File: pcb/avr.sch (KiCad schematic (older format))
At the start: 33 parts, among them IC201 MCU-ATMEGA328P-MU_QFN32_, J201 CONN_02X03, P201 CONNECTOR, P202 CONNECTOR, P203 CONNECTOR, P204 CONNECTOR, P205 CONNECTOR, P206 CONNECTOR, P207 CONNECTOR, P208 CONNECTOR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

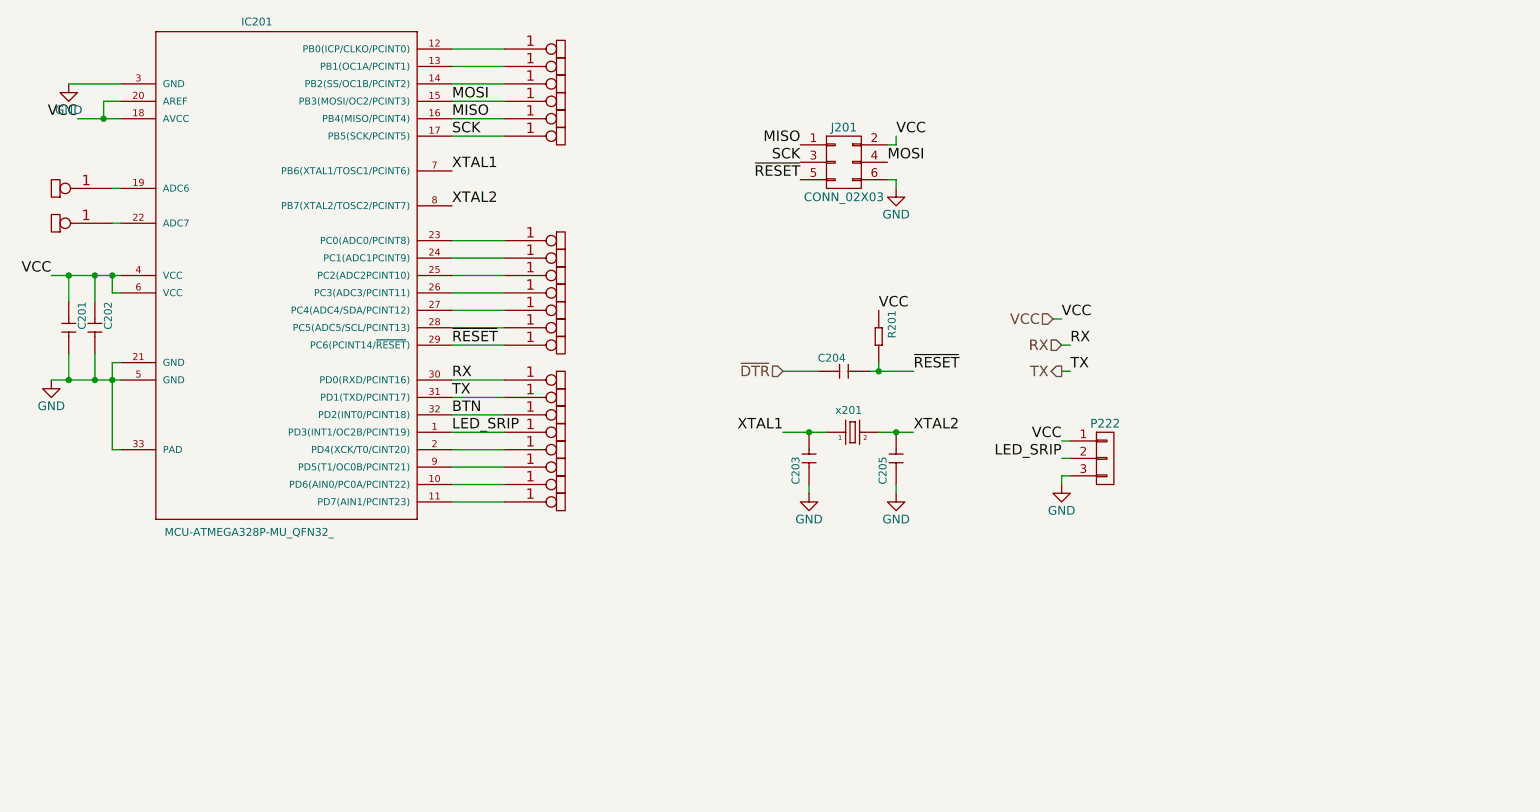
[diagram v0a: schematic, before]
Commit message: added led strip power control, minor adjustments to layout
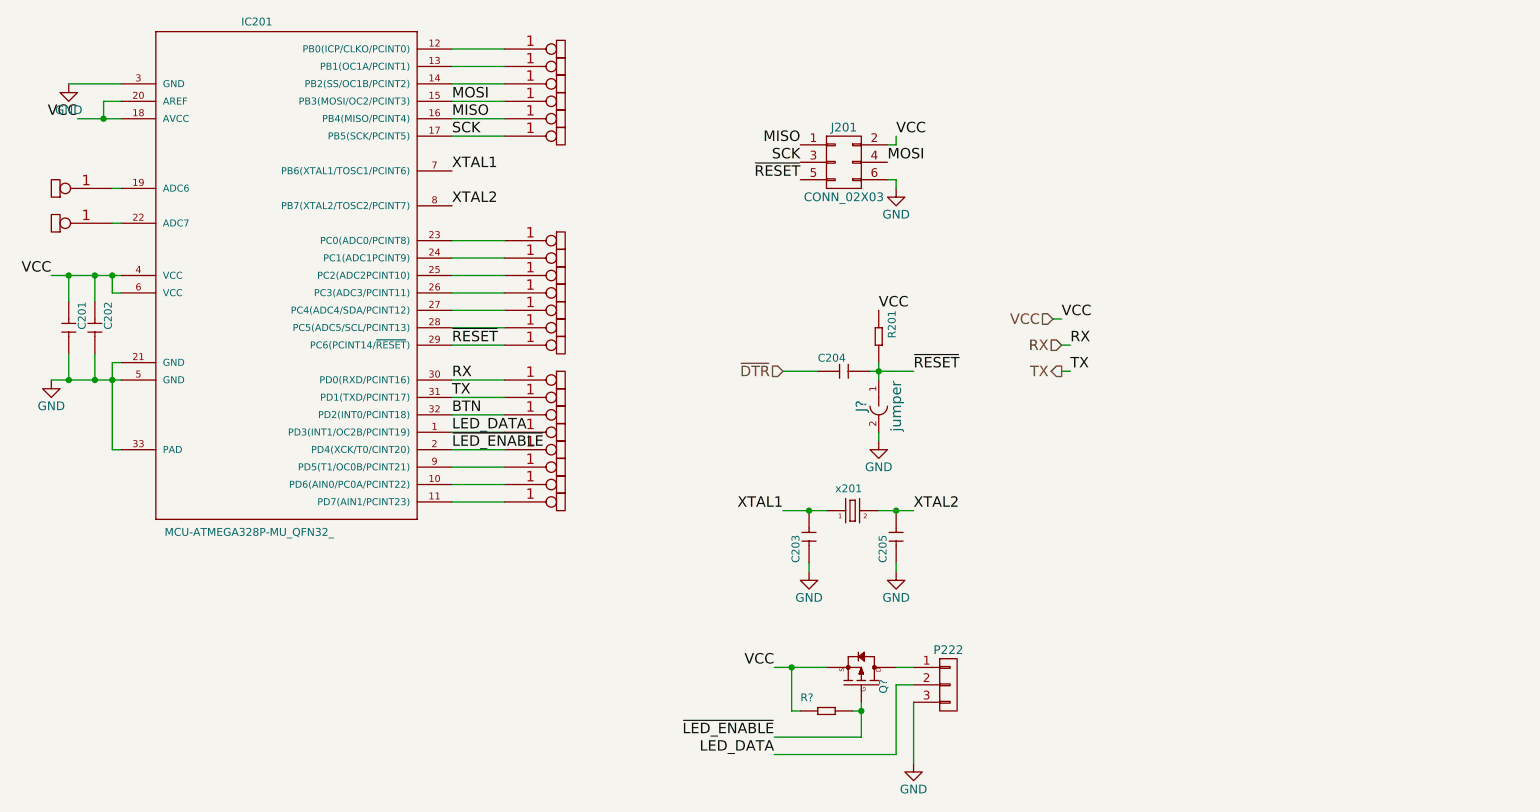
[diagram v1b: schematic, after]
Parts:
- added J?: jumper, symbol jumper
- added Q?: SMD-MOSFET-P-CH-8V-4.1A-CJ2305_SOT-23_, SeeedOPL-Transistor-2016:SOT-23, symbol SMD-MOSFET-P-CH-8V-4.1A-CJ2305_SOT-23_
- added R?: SMD-RES-10K-1%-1_10W_0603_, SeeedOPL-Resistor-2016:R0603, symbol SMD-RES-10K-1%-1_10W_0603_
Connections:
- net GND: now also J?.2
- net VCC: now also Q?.2 (S), R?.1; no longer P222.1 (P1)
- net ~RESET: now also J?.1
- net ~LED_ENABLE: now reaches IC201.2 (PD4(XCK/T0/CINT20)), P218.1 (W)
- net ~LED_ENABLE: now also Q?.1 (G), R?.2
- net LED_SRIP renamed LED_DATA
- new net: P222.1 (P1), Q?.3 (D)
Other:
- moved on the sheet: C203, C205, P222, x201

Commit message: layout mostly done
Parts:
- gave numbers to parts that had none: 3
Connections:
- net VCC: no longer IC201.20 (AREF)
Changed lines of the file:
@@
 $EndComp
 $Comp
-L GND #PWR05
+L GND #PWR207
 U 1 1 58BAB3DE
 P 8050 6250
-F 0 "#PWR05" H 8050 6000 50  0001 C CNN
+F 0 "#PWR207" H 8050 6000 50  0001 C CNN
 F 1 "GND" H 8050 6100 50  0000 C CNN
 F 2 "" H 8050 6250 50  0000 C CNN
@@
 $EndComp
 $Comp
-L GND #PWR06
+L GND #PWR206
 U 1 1 5A3AC4B3
 P 7950 5150
-F 0 "#PWR06" H 7950 4900 50  0001 C CNN
+F 0 "#PWR206" H 7950 4900 50  0001 C CNN
 F 1 "GND" H 7950 5000 50  0000 C CNN
 F 2 "" H 7950 5150 50  0000 C CNN
@@
 $EndComp
 $Comp
-L GND #PWR07
+L GND #PWR203
 U 1 1 5A3AC530
 P 7450 5150
-F 0 "#PWR07" H 7450 4900 50  0001 C CNN
+F 0 "#PWR203" H 7450 4900 50  0001 C CNN
 F 1 "GND" H 7450 5000 50  0000 C CNN
 F 2 "" H 7450 5150 50  0000 C CNN
@@
 $EndComp
 $Comp
-L GND #PWR08
+L GND #PWR201
 U 1 1 5A3AD1F6
 P 3100 4050
-F 0 "#PWR08" H 3100 3800 50  0001 C CNN
+F 0 "#PWR201" H 3100 3800 50  0001 C CNN
 F 1 "GND" H 3100 3900 50  0000 C CNN
 F 2 "" H 3100 4050 50  0001 C CNN
@@
 $EndComp
 $Comp
-L GND #PWR09
+L GND #PWR202
 U 1 1 5A3AE5DA
 P 3200 2350
-F 0 "#PWR09" H 3200 2100 50  0001 C CNN
+F 0 "#PWR202" H 3200 2100 50  0001 C CNN
 F 1 "GND" H 3200 2200 50  0000 C CNN
 F 2 "" H 3200 2350 50  0001 C CNN
@@
 SCK
 $Comp
-L GND #PWR010
+L GND #PWR205
 U 1 1 5A551E4E
 P 7950 2950
-F 0 "#PWR010" H 7950 2700 50  0001 C CNN
+F 0 "#PWR205" H 7950 2700 50  0001 C CNN
 F 1 "GND" H 7950 2800 50  0000 C CNN
 F 2 "" H 7950 2950 50  0000 C CNN
@@
 VCC
 $Comp
-L SMD-MOSFET-P-CH-8V-4.1A-CJ2305_SOT-23_ Q?
+L SMD-MOSFET-P-CH-8V-4.1A-CJ2305_SOT-23_ Q201
 U 1 1 5A56622B
 P 7750 5700
-F 0 "Q?" H 7600 5800 45  0000 L BNN
+F 0 "Q201" H 7600 5800 45  0000 L BNN
 F 1 "SMD-MOSFET-P-CH-8V-4.1A-CJ2305_SOT-23_" H 7750 5800 45  0001 L BNN
 F 2 "SeeedOPL-Transistor-2016:SOT-23" H 7750 5700 60  0001 C CNN
@@
 VCC
 $Comp
-L SMD-RES-10K-1%-1_10W_0603_ R?
+L SMD-RES-10K-1%-1_10W_0603_ R202
 U 1 1 5A56659F
 P 7550 5950
-F 0 "R?" H 7400 6000 45  0000 L BNN
+F 0 "R202" H 7400 6000 45  0000 L BNN
 F 1 "SMD-RES-10K-1%-1_10W_0603_" H 7400 5850 45  0001 L BNN
 F 2 "SeeedOPL-Resistor-2016:R0603" H 7550 5950 40  0001 C CNN
@@
 	7950 5700 8050 5700
 Wire Wire Line
-	7300 4800 7450 4800
-Wire Wire Line
-	7450 4800 7550 4800
-Wire Wire Line
-	7850 4800 7950 4800
-Wire Wire Line
-	7950 4800 8050 4800
+	7300 4800 7550 4800
+Wire Wire Line
+	7850 4800 8050 4800
 Wire Wire Line
 	7450 5100 7450 5150
@@
 Connection ~ 7950 4800
 Wire Wire Line
-	3100 3450 3200 3450
-Wire Wire Line
-	3200 3450 3350 3450
-Wire Wire Line
-	3350 3450 3450 3450
-Wire Wire Line
-	3450 3450 3500 3450
+	3100 3450 3500 3450
 Wire Wire Line
 	3200 3600 3200 3450
@@
 Connection ~ 3450 3450
 Wire Wire Line
-	3100 4050 3200 4050
-Wire Wire Line
-	3200 4050 3350 4050
-Wire Wire Line
-	3350 4050 3450 4050
-Wire Wire Line
-	3450 4050 3500 4050
+	3100 4050 3500 4050
 Wire Wire Line
 	3200 3900 3200 4050
@@
 	3500 3950 3450 3950
 Wire Wire Line
-	3450 3950 3450 4050
-Wire Wire Line
-	3450 4050 3450 4450
+	3450 3950 3450 4450
 Connection ~ 3450 4050
 Wire Wire Line
-	3250 2550 3400 2550
-Wire Wire Line
-	3400 2550 3500 2550
-Wire Wire Line
 	3500 2350 3200 2350
 Wire Wire Line
-	3500 2450 3400 2450
-Wire Wire Line
-	3400 2450 3400 2550
-Connection ~ 3400 2550
-Wire Wire Line
 	5400 4050 5700 4050
 Wire Wire Line
 	5400 4150 5700 4150
 Wire Wire Line
-	7850 3950 7850 4000
-Wire Wire Line
-	7850 4000 7850 4050
-Wire Wire Line
-	7800 4000 7850 4000
-Wire Wire Line
-	7850 4000 8050 4000
+	7850 3950 7850 4050
+Wire Wire Line
+	7800 4000 8050 4000
 Connection ~ 7850 4000
 Wire Wire Line
@@
 	8850 3700 8900 3700
 Wire Wire Line
-	7250 5700 7350 5700
-Wire Wire Line
-	7350 5700 7550 5700
-Wire Wire Line
-	7750 5900 7750 5950
-Wire Wire Line
-	7750 5950 7750 6100
+	7250 5700 7550 5700
+Wire Wire Line
+	7750 5900 7750 6100
 Wire Wire Line
 	7750 5950 7700 5950
@@
 ~LED_ENABLE
 $Comp
-L jumper J?
+L jumper J202
 U 1 1 5A566ADC
 P 7850 4200
-F 0 "J?" H 7850 4100 60  0000 C CNN
+F 0 "J202" H 7850 4100 60  0000 C CNN
 F 1 "jumper" H 7850 4300 60  0000 C CNN
 F 2 "" H 7850 4200 60  0000 C CNN
@@
 $EndComp
 $Comp
-L GND #PWR?
+L GND #PWR204
 U 1 1 5A566D1F
 P 7850 4400
-F 0 "#PWR?" H 7850 4150 50  0001 C CNN
+F 0 "#PWR204" H 7850 4150 50  0001 C CNN
 F 1 "GND" H 7850 4250 50  0000 C CNN
 F 2 "" H 7850 4400 50  0000 C CNN
@@
 Wire Wire Line
 	7950 6200 7950 5800
+Wire Wire Line
+	3250 2550 3500 2550
+Wire Wire Line
+	3500 2450 3450 2450
 $EndSCHEMATC
